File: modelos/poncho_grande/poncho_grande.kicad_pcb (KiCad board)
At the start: 2 copper layers, 85.7 x 137.2 mm, 25 parts, among them P1 CONN_02X20, P10 CONN_01X20, P11 CONN_01X20, P12 CONN_01X06, P13 CONN_01X06, P14 CONN_02X12, P15 CONN_02X12, P16 CONN_02X12, P17 CONN_02X12, P18 CONN_01X12, P19 CONN_01X12, P2 CONN_01X20, P20 CONN_01X12, P21 CONN_01X12, P3 CONN_02X20, P4 CONN_02X20, P5 CONN_01X19, P6 CONN_02X20, P7 CONN_01X20, P8 CONN_02X20, P9 CONN_02X20

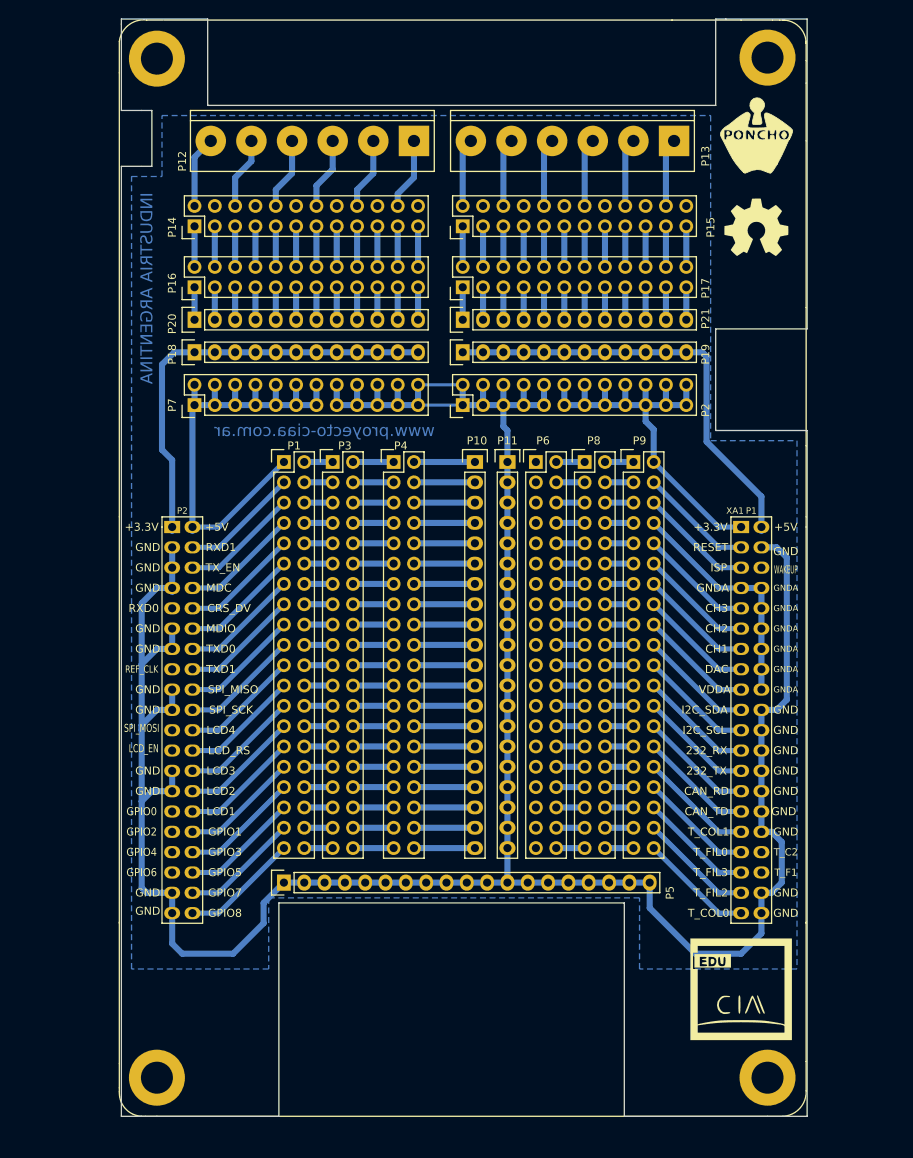
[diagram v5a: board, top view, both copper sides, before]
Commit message: * Modificaciones estéticas y de leyendas al diseño.
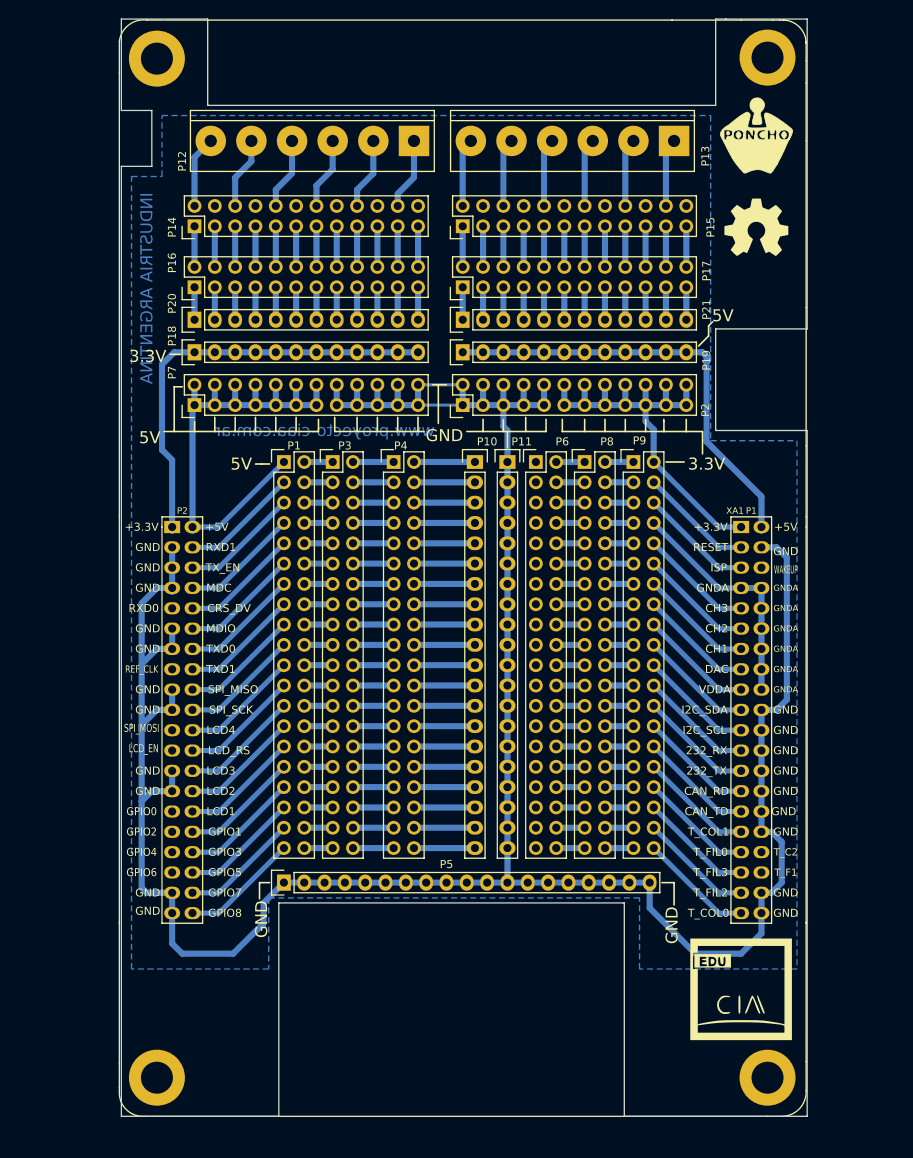
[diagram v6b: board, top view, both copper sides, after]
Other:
- board text added: "3.3V"
- board text added: "5V"
- board text added: "GND"
- board text added: "PONCHO GRANDE http://www.proyecto-ciaa.com.ar/"
- board text removed: "PENDIENTES: * Colocar serigrafía para indicar señales y alimentaciones en el área de prototipado."
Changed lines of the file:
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@@
-(kicad_pcb (version 4) (host pcbnew "(2015-05-19 BZR 5670)-product")
+(kicad_pcb (version 4) (host pcbnew "(2015-08-26 BZR 6128)-product")
   (general
     (links 337)
@@
     (area 73.584999 25.324999 159.460001 162.635001)
     (thickness 1.6)
-    (drawings 32)
+    (drawings 88)
     (tracks 437)
     (zones 0)
@@
   (page A4)
   (title_block
-    (title "Poncho Grande - Modelo / Ejemplo")
+    (title "Poncho Grande - Modelo - Ejemplo - Template")
     (date "mar 29 sep 2015")
     (rev 1.0)
@@
   (layers
     (0 F.Cu signal)
-    (31 B.Cu signal)
+    (31 B.Cu signal hide)
     (32 B.Adhes user)
     (33 F.Adhes user)
@@
     (descr "Through hole pin header")
     (tags "pin header")
-    (fp_text reference P6 (at 0.889 -2.667) (layer F.SilkS)
+    (fp_text reference P6 (at 3.302 -2.54) (layer F.SilkS)
       (effects (font (size 1 1) (thickness 0.15)))
     )
@@
     (descr "Through hole pin header")
     (tags "pin header")
-    (fp_text reference P8 (at 1.143 -2.667) (layer F.SilkS)
+    (fp_text reference P8 (at 2.794 -2.54) (layer F.SilkS)
       (effects (font (size 1 1) (thickness 0.15)))
     )
@@
     (descr "Through hole pin header")
     (tags "pin header")
-    (fp_text reference P10 (at 0.254 -2.667) (layer F.SilkS)
+    (fp_text reference P10 (at 1.524 -2.54) (layer F.SilkS)
       (effects (font (size 1 1) (thickness 0.15)))
     )
@@
     (descr "Through hole pin header")
     (tags "pin header")
-    (fp_text reference P11 (at 0 -2.667) (layer F.SilkS)
+    (fp_text reference P11 (at 1.778 -2.54) (layer F.SilkS)
       (effects (font (size 1 1) (thickness 0.15)))
     )
@@
     (descr "Through hole pin header")
     (tags "pin header")
-    (fp_text reference P7 (at 0 -2.794 90) (layer F.SilkS)
+    (fp_text reference P7 (at 4.064 -2.794 90) (layer F.SilkS)
       (effects (font (size 1 1) (thickness 0.15)))
     )
@@
     (descr "Through hole pin header")
     (tags "pin header")
-    (fp_text reference P16 (at 0.508 -2.794 90) (layer F.SilkS)
+    (fp_text reference P16 (at 3.048 -2.794 90) (layer F.SilkS)
       (effects (font (size 1 1) (thickness 0.15)))
     )
@@
     (descr "Through hole pin header")
     (tags "pin header")
-    (fp_text reference P17 (at -0.127 30.353 90) (layer F.SilkS)
+    (fp_text reference P17 (at 2.032 30.48 90) (layer F.SilkS)
       (effects (font (size 1 1) (thickness 0.15)))
     )
@@
     (descr "Through hole pin header")
     (tags "pin header")
-    (fp_text reference P18 (at -0.254 -2.794 90) (layer F.SilkS)
+    (fp_text reference P18 (at 2.032 -2.794 90) (layer F.SilkS)
       (effects (font (size 1 1) (thickness 0.15)))
     )
@@
     (descr "Through hole pin header")
     (tags "pin header")
-    (fp_text reference P19 (at -0.254 30.353 270) (layer F.SilkS)
+    (fp_text reference P19 (at -1.016 30.48 270) (layer F.SilkS)
       (effects (font (size 1 1) (thickness 0.15)))
     )
@@
     (descr "Through hole pin header")
     (tags "pin header")
-    (fp_text reference P20 (at -0.508 -2.794 90) (layer F.SilkS)
+    (fp_text reference P20 (at 2.032 -2.794 90) (layer F.SilkS)
       (effects (font (size 1 1) (thickness 0.15)))
     )
@@
     (descr "Through hole pin header")
     (tags "pin header")
-    (fp_text reference P21 (at 0.127 30.353 90) (layer F.SilkS)
+    (fp_text reference P21 (at 1.27 30.48 90) (layer F.SilkS)
       (effects (font (size 1 1) (thickness 0.15)))
     )
@@
     (descr "Through hole pin header")
     (tags "pin header")
-    (fp_text reference P5 (at -1.27 48.26 90) (layer F.SilkS)
+    (fp_text reference P5 (at 2.286 20.32 180) (layer F.SilkS)
       (effects (font (size 1 1) (thickness 0.15)))
     )
@@
       (xy -3.33756 -3.59918) (xy -3.33756 -3.59918)) (layer F.SilkS) (width 0.00254))
   )
-  (gr_text "PENDIENTES: \n* Colocar serigrafía para indicar señales y \nalimentaciones en el área de prototipado.\n" (at 191.77 63.5) (layer Dwgs.User)
+  (gr_line (start 146.304 76.962) (end 146.304 79.756) (angle 90) (layer F.SilkS) (width 0.2))
+  (gr_line (start 144.272 76.962) (end 146.304 76.962) (angle 90) (layer F.SilkS) (width 0.2))
+  (gr_line (start 141.478 75.692) (end 141.478 75.438) (angle 90) (layer F.SilkS) (width 0.2))
+  (gr_line (start 144.272 76.962) (end 144.272 75.438) (angle 90) (layer F.SilkS) (width 0.2))
+  (gr_line (start 141.478 76.962) (end 144.272 76.962) (angle 90) (layer F.SilkS) (width 0.2))
+  (gr_line (start 141.478 76.962) (end 141.478 75.692) (angle 90) (layer F.SilkS) (width 0.2))
+  (gr_line (start 139.192 75.438) (end 139.192 76.962) (angle 90) (layer F.SilkS) (width 0.2))
+  (gr_line (start 136.652 75.438) (end 136.652 76.962) (angle 90) (layer F.SilkS) (width 0.2))
+  (gr_line (start 134.112 75.438) (end 134.112 76.962) (angle 90) (layer F.SilkS) (width 0.2))
+  (gr_line (start 131.572 75.438) (end 131.572 76.962) (angle 90) (layer F.SilkS) (width 0.2))
+  (gr_line (start 128.778 76.962) (end 128.778 75.438) (angle 90) (layer F.SilkS) (width 0.2))
+  (gr_line (start 141.478 76.962) (end 128.778 76.962) (angle 90) (layer F.SilkS) (width 0.2))
+  (gr_text 3.3V (at 146.812 81.026) (layer F.SilkS)
     (effects (font (size 1.5 1.5) (thickness 0.3)))
   )
+  (gr_line (start 141.732 80.772) (end 144.018 80.772) (angle 90) (layer F.SilkS) (width 0.2))
+  (gr_line (start 91.186 81.026) (end 90.424 81.026) (angle 90) (layer F.SilkS) (width 0.2))
+  (gr_line (start 91.186 81.026) (end 92.202 81.026) (angle 90) (layer F.SilkS) (width 0.2))
+  (gr_text 5V (at 88.646 81.026) (layer F.SilkS)
+    (effects (font (size 1.5 1.5) (thickness 0.3)))
+  )
+  (gr_line (start 142.748 133.35) (end 141.224 133.35) (angle 90) (layer F.SilkS) (width 0.2))
+  (gr_line (start 142.748 136.144) (end 142.748 133.35) (angle 90) (layer F.SilkS) (width 0.2))
+  (gr_text GND (at 142.494 138.684 90) (layer F.SilkS)
+    (effects (font (size 1.5 1.5) (thickness 0.3)))
+  )
+  (gr_line (start 90.932 133.35) (end 92.202 133.35) (angle 90) (layer F.SilkS) (width 0.2))
+  (gr_line (start 90.932 135.382) (end 90.932 133.35) (angle 90) (layer F.SilkS) (width 0.2))
+  (gr_text GND (at 91.186 137.922 90) (layer F.SilkS)
+    (effects (font (size 1.5 1.5) (thickness 0.3)))
+  )
+  (gr_line (start 121.92 76.962) (end 121.92 78.994) (angle 90) (layer F.SilkS) (width 0.2))
+  (gr_line (start 80.264 71.374) (end 81.28 71.374) (angle 90) (layer F.SilkS) (width 0.2))
+  (gr_line (start 80.264 76.962) (end 80.264 71.374) (angle 90) (layer F.SilkS) (width 0.2))
+  (gr_line (start 95.504 76.962) (end 95.504 75.184) (angle 90) (layer F.SilkS) (width 0.2))
+  (gr_line (start 92.964 76.962) (end 92.964 75.184) (angle 90) (layer F.SilkS) (width 0.2))
+  (gr_line (start 90.424 76.962) (end 90.424 75.184) (angle 90) (layer F.SilkS) (width 0.2))
+  (gr_line (start 87.884 76.962) (end 87.884 75.184) (angle 90) (layer F.SilkS) (width 0.2))
+  (gr_line (start 85.344 76.962) (end 85.344 75.184) (angle 90) (layer F.SilkS) (width 0.2))
+  (gr_line (start 82.804 76.962) (end 82.804 75.692) (angle 90) (layer F.SilkS) (width 0.2))
+  (gr_line (start 98.298 76.962) (end 78.994 76.962) (angle 90) (layer F.SilkS) (width 0.2))
+  (gr_line (start 98.298 76.962) (end 98.298 75.438) (angle 90) (layer F.SilkS) (width 0.2))
+  (gr_text 5V (at 77.216 77.724) (layer F.SilkS)
+    (effects (font (size 1.5 1.5) (thickness 0.3)))
+  )
+  (gr_line (start 79.756 67.31) (end 81.026 67.31) (angle 90) (layer F.SilkS) (width 0.2))
+  (gr_text 3.3V (at 76.962 67.564) (layer F.SilkS)
+    (effects (font (size 1.5 1.5) (thickness 0.3)))
+  )
+  (gr_line (start 118.872 76.962) (end 118.872 75.438) (angle 90) (layer F.SilkS) (width 0.2))
+  (gr_line (start 121.412 76.962) (end 121.412 75.438) (angle 90) (layer F.SilkS) (width 0.2))
+  (gr_line (start 124.206 76.962) (end 124.206 75.184) (angle 90) (layer F.SilkS) (width 0.2))
+  (gr_line (start 126.746 76.962) (end 126.746 75.438) (angle 90) (layer F.SilkS) (width 0.2))
+  (gr_line (start 116.84 76.962) (end 126.746 76.962) (angle 90) (layer F.SilkS) (width 0.2))
+  (gr_line (start 113.284 71.12) (end 114.3 71.12) (angle 90) (layer F.SilkS) (width 0.2))
+  (gr_line (start 113.284 71.12) (end 113.284 75.946) (angle 90) (layer F.SilkS) (width 0.2))
+  (gr_line (start 112.522 71.12) (end 113.284 71.12) (angle 90) (layer F.SilkS) (width 0.2))
+  (gr_line (start 110.744 76.962) (end 110.744 75.184) (angle 90) (layer F.SilkS) (width 0.2))
+  (gr_line (start 108.204 75.184) (end 108.204 76.962) (angle 90) (layer F.SilkS) (width 0.2))
+  (gr_line (start 105.664 75.184) (end 105.664 76.962) (angle 90) (layer F.SilkS) (width 0.2))
+  (gr_line (start 103.124 75.184) (end 103.124 76.962) (angle 90) (layer F.SilkS) (width 0.2))
+  (gr_line (start 100.33 76.962) (end 100.33 75.184) (angle 90) (layer F.SilkS) (width 0.2))
+  (gr_line (start 111.506 76.962) (end 100.33 76.962) (angle 90) (layer F.SilkS) (width 0.2))
+  (gr_text GND (at 114.046 77.47) (layer F.SilkS)
+    (effects (font (size 1.5 1.5) (thickness 0.3)))
+  )
+  (gr_line (start 147.066 63.754) (end 147.574 63.246) (angle 90) (layer F.SilkS) (width 0.2))
+  (gr_line (start 147.066 65.024) (end 147.066 63.754) (angle 90) (layer F.SilkS) (width 0.2))
+  (gr_line (start 145.796 66.294) (end 147.066 65.024) (angle 90) (layer F.SilkS) (width 0.2))
+  (gr_text 5V (at 148.844 62.484) (layer F.SilkS)
+    (effects (font (size 1.5 1.5) (thickness 0.3)))
+  )
+  (gr_text "PONCHO GRANDE\nhttp://www.proyecto-ciaa.com.ar/" (at 113.538 30.734) (layer Dwgs.User)
+    (effects (font (size 1.5 1.5) (thickness 0.3)))
+  )

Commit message: * Modifico textos de licencia en rótulos y archivos.
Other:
- board text added: "Borrar la Plantilla-EDU-CIAA al finalizar el posicionamiento y el borde de PCB."
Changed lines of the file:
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@@
     (links 337)
     (no_connects 0)
-    (area 73.584999 25.324999 159.460001 162.635001)
+    (area 54.087144 24.920279 177.608572 182.405001)
     (thickness 1.6)
-    (drawings 88)
+    (drawings 92)
     (tracks 437)
     (zones 0)
@@
     (rev 1.0)
     (company "Proyecto CIAA - COMPUTADORA INDUSTRIAL ABIERTA ARGENTINA")
-    (comment 1 "Autores: Ver '../doc/CAMBIOS.txt'   Licencia: Ver '../doc/LICENCIA.txt'")
+    (comment 1 https://github.com/ciaa/Ponchos/tree/master/modelos/doc)
+    (comment 2 "Autores y Licencias ver el siguiente enlace:")
   )
   (layers
@@
       (xy -3.33756 -3.59918) (xy -3.33756 -3.59918)) (layer F.SilkS) (width 0.00254))
   )
+  (gr_line (start 160.02 68.58) (end 161.29 69.215) (angle 90) (layer Dwgs.User) (width 0.2))
+  (gr_line (start 160.02 68.58) (end 161.29 67.945) (angle 90) (layer Dwgs.User) (width 0.2))
+  (gr_line (start 160.02 68.58) (end 167.64 68.58) (angle 90) (layer Dwgs.User) (width 0.2))
+  (gr_text "Borrar la Plantilla-EDU-CIAA al finalizar \nel posicionamiento y el borde de PCB.\n" (at 192.405 69.85) (layer Dwgs.User)
+    (effects (font (size 1.5 1.5) (thickness 0.3)))
+  )
   (gr_line (start 146.304 76.962) (end 146.304 79.756) (angle 90) (layer F.SilkS) (width 0.2))
